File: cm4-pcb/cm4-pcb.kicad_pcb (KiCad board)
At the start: 2 copper layers, 140 x 70.5 mm, 41 parts, among them J1 Conn_01x02_Pin, J2 Conn_01x02_Pin, J3 USB1125-GF-B, J4 Conn_02x03_Odd_Even, J5 Conn_01x04, J6 Conn_01x04, J7 Conn_01x02, U1 Pfostenstecker_6_2x3, U2 Pfostenstecker_6_2x3, U3 TPD4EUSB30, U4 MagJack-A70-112-331N126, U5 SMD-PUSH-BTN, U6 TPD4EUSB30, U7 TPD4EUSB30

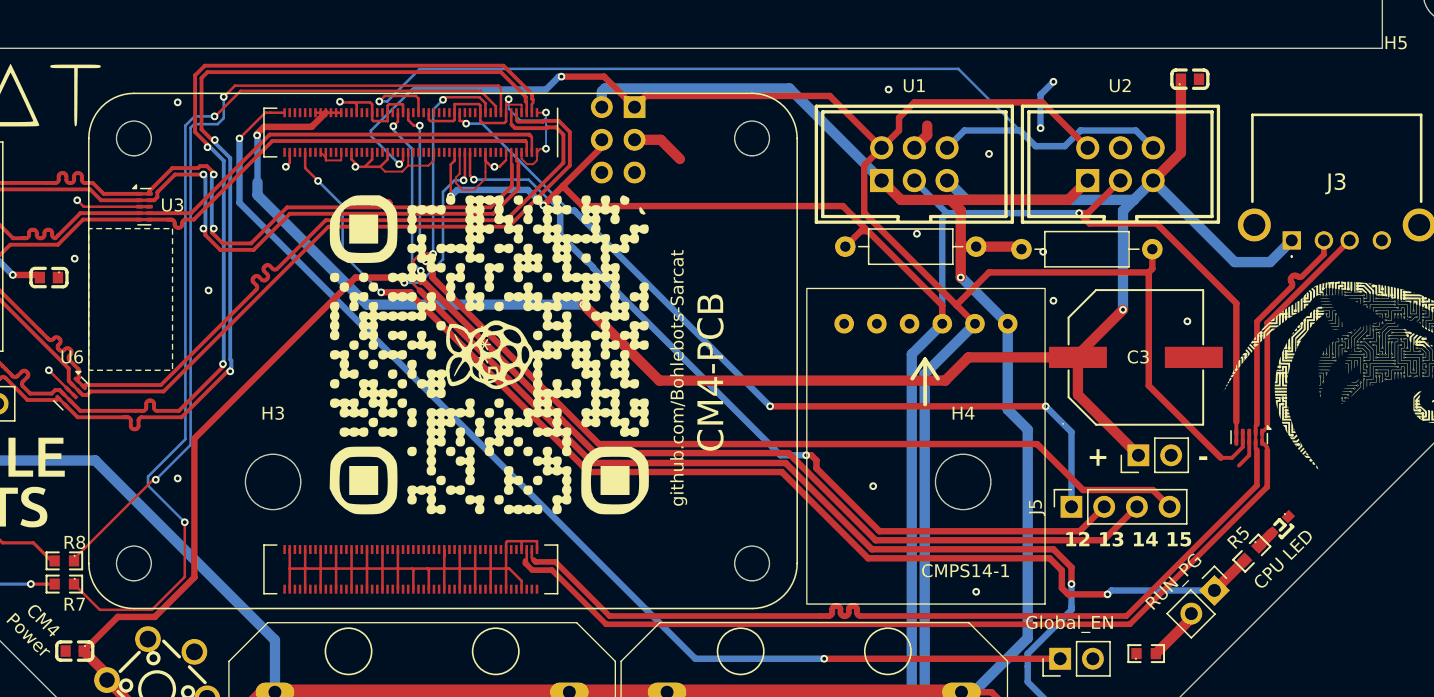
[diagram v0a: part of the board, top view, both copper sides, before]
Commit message: Moved Diff. Pair Routes for Crosstalk
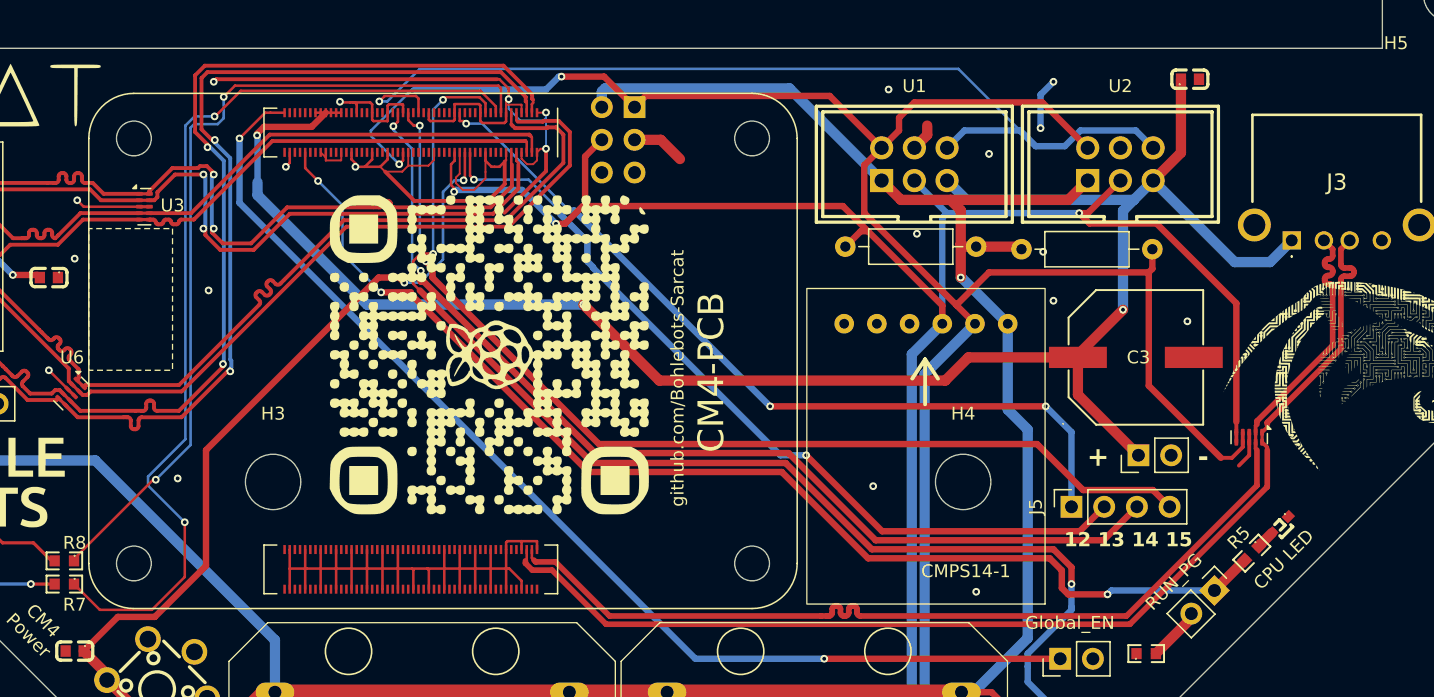
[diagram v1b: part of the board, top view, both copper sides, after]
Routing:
- net GND: track 203.1 -> 245.5 mm, vias 23 -> 22
- net USB_D+: track 87.2 -> 88.7 mm
- net USB_D-: track 87.1 -> 88.6 mm
- net SHUTDOWN: track 70.5 -> 69.5 mm
- net SCL: track 199.1 -> 199.7 mm

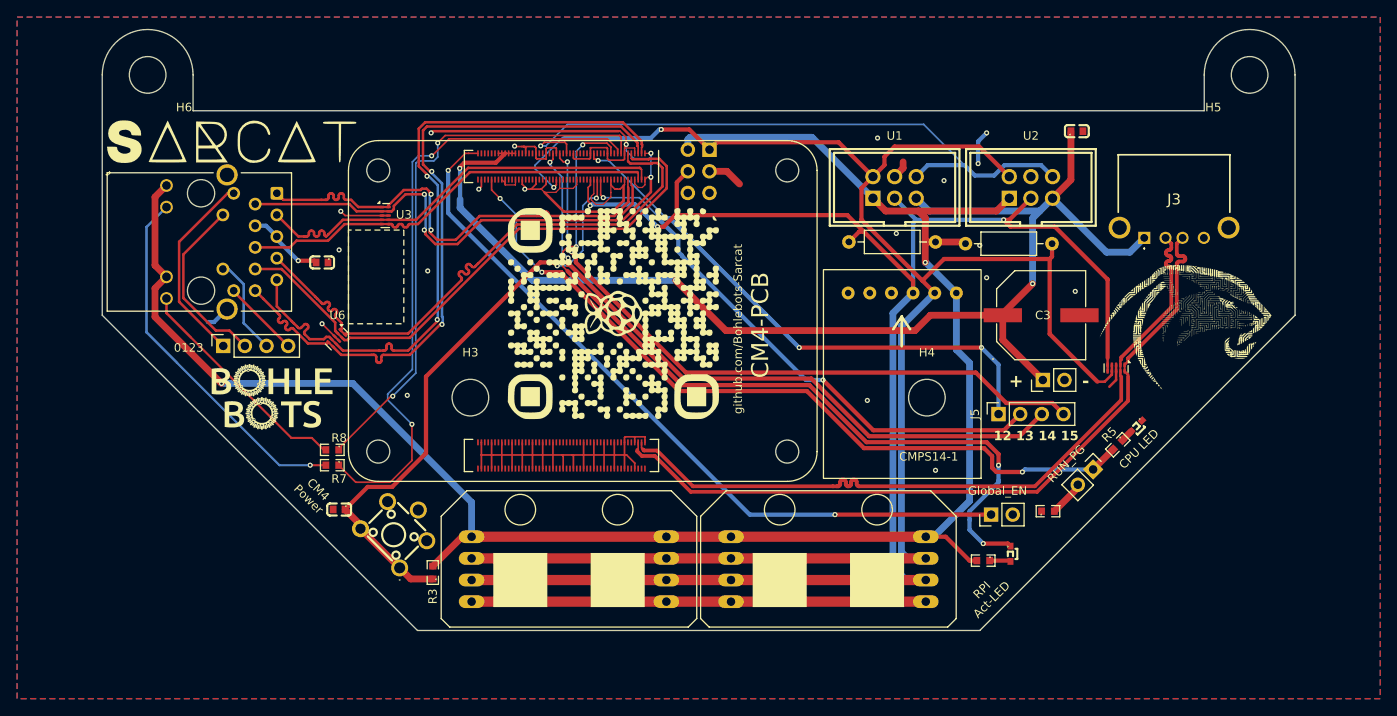
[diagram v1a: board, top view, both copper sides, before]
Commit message: Changed Ethernet Magjack + some layout changes
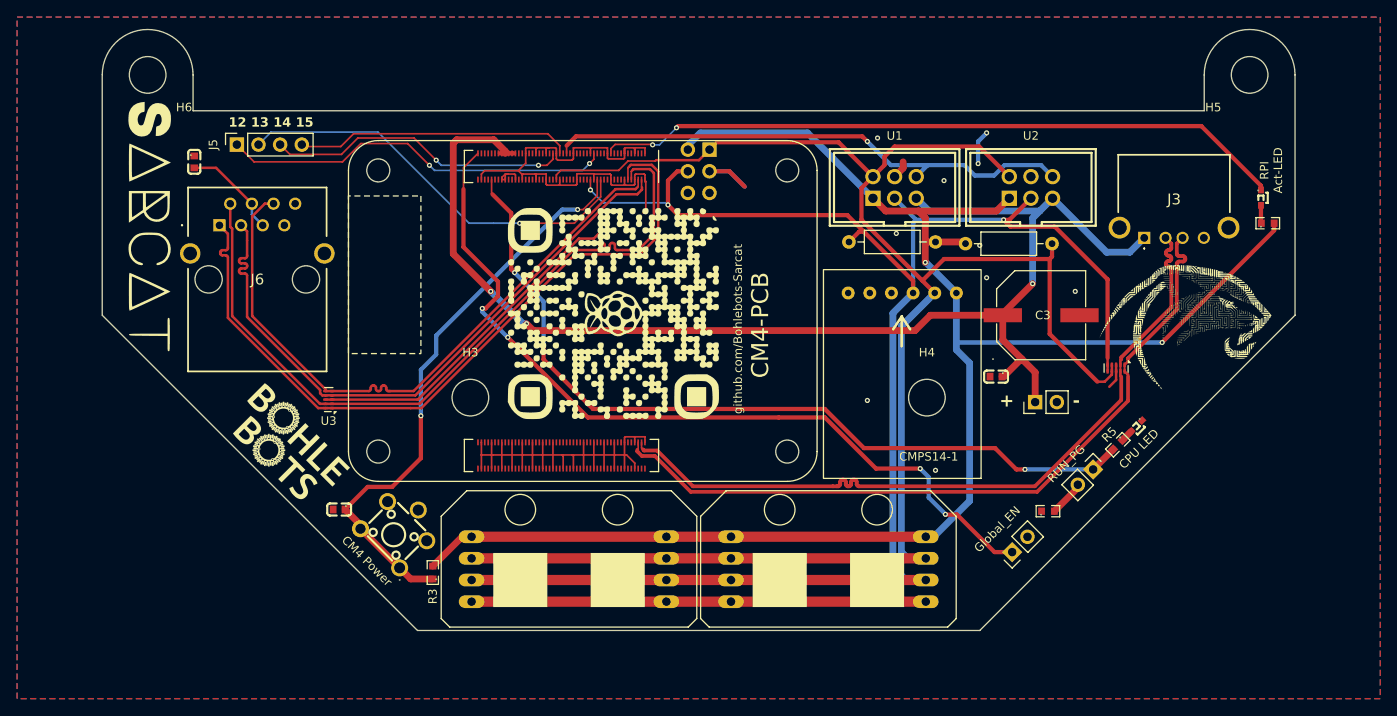
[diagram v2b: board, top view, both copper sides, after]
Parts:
- removed R7, R8: SMD-470R, BohleBots:R0603
- removed U4: MagJack-A70-112-331N126, CM4IO:TRJG0926HENL
- removed U6: TPD4EUSB30, Package_SON:USON-10_2.5x1.0mm_P0.5mm
- J6: value Conn_01x04 -> J0011D21NL; footprint Connector_PinSocket_2.54mm:PinSocket_1x04_P2.54mm_Vertical -> J0011D21NL:J0011D21NL
- moved J5 94.8 mm to (-54.2, 35.0)
- moved R6 51.8 mm to (66.8, 44.2), turned to 0 degrees
- moved ACT_LED1 51.1 mm to (66.0, 41.2)
- moved C4 30.3 mm to (34.9, 62.2), turned to 180 degrees
- moved U3 22.6 mm to (-43.4, 64.9), turned to 180 degrees
- moved C1 19.1 mm to (-59.2, 37.0), turned to -90 degrees
- moved J6 14.2 mm to (-56.2, 44.4), turned to 180 degrees
- moved G*** 13.9 mm to (-64.4, 44.6), turned to -90 degrees
- moved G*** 5.93 mm to (-48.3, 70.2), turned to -45 degrees
- moved J1 5.05 mm to (36.8, 82.8), turned to 135 degrees
- moved J7 2.75 mm to (39.5, 65.2)
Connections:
- C1 pad 2: Net-(C1-Pad2) -> Net-(J6-CT_1)
- J6 pad 1: /TR0_TAP -> /TRD0_P
- J6 pad 2: /TR1_TAP -> /TRD0_N
- J6 pad 3: /TR2_TAP -> /TRD1_P
- J6 pad 4: /TR3_TAP -> Net-(J6-CT_1)
- Module1 pad 11: /TRD2_P -> unconnected-(Module1A-Ethernet_Pair2_P-Pad11)
- Module1 pad 15: /ETH_LEDY -> unconnected-(Module1A-Ethernet_nLED3(3.3v)-Pad15)
- Module1 pad 17: /ETH_LEDG -> unconnected-(Module1A-Ethernet_nLED2(3.3v)-Pad17)
- Module1 pad 3: /TRD3_P -> unconnected-(Module1A-Ethernet_Pair3_P-Pad3)
- Module1 pad 5: /TRD3_N -> unconnected-(Module1A-Ethernet_Pair3_N-Pad5)
- Module1 pad 9: /TRD2_N -> unconnected-(Module1A-Ethernet_Pair2_N-Pad9)
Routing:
- net /TRD3_P: track 81.0 -> 0.00 mm, vias 2 -> 0
- net /TRD3_N: track 81.0 -> 0.00 mm, vias 2 -> 0
- net /ETH_LEDG: track 74.1 -> 0.00 mm, vias 2 -> 0
- net /TRD2_P: track 68.5 -> 0.00 mm
- net /TRD2_N: track 67.5 -> 0.00 mm
- net /ETH_LEDY: track 65.9 -> 0.00 mm, vias 2 -> 0
- net P15: track 78.5 -> 32.5 mm, vias 2 -> 0
- net P14: track 79.1 -> 35.6 mm
- net Net-(U4-LEDG_K): track 43.2 -> 0.00 mm, vias 1 -> 0
- net /TRD0_P: track 55.7 -> 88.9 mm, vias 2 -> 0
- net /TRD0_N: track 55.8 -> 88.8 mm, vias 2 -> 0
- net +3.3V: track 225.3 -> 194.5 mm
- net Net-(U4-LEDY_K): track 27.1 -> 0.00 mm
- net /TRD1_N: track 50.2 -> 76.3 mm
- net /TRD1_P: track 50.2 -> 75.5 mm
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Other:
- board text removed: "0123"

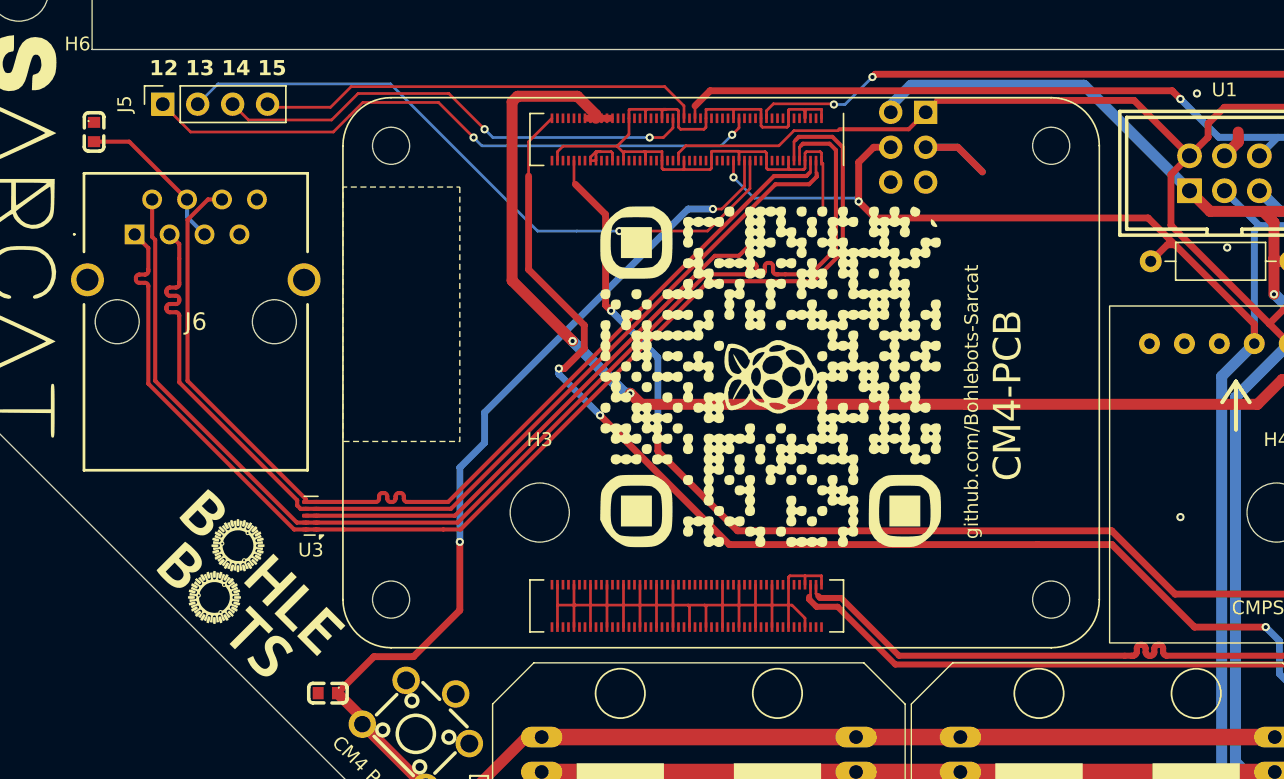
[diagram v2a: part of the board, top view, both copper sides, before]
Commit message: Adjusted GND Layer for Antenna
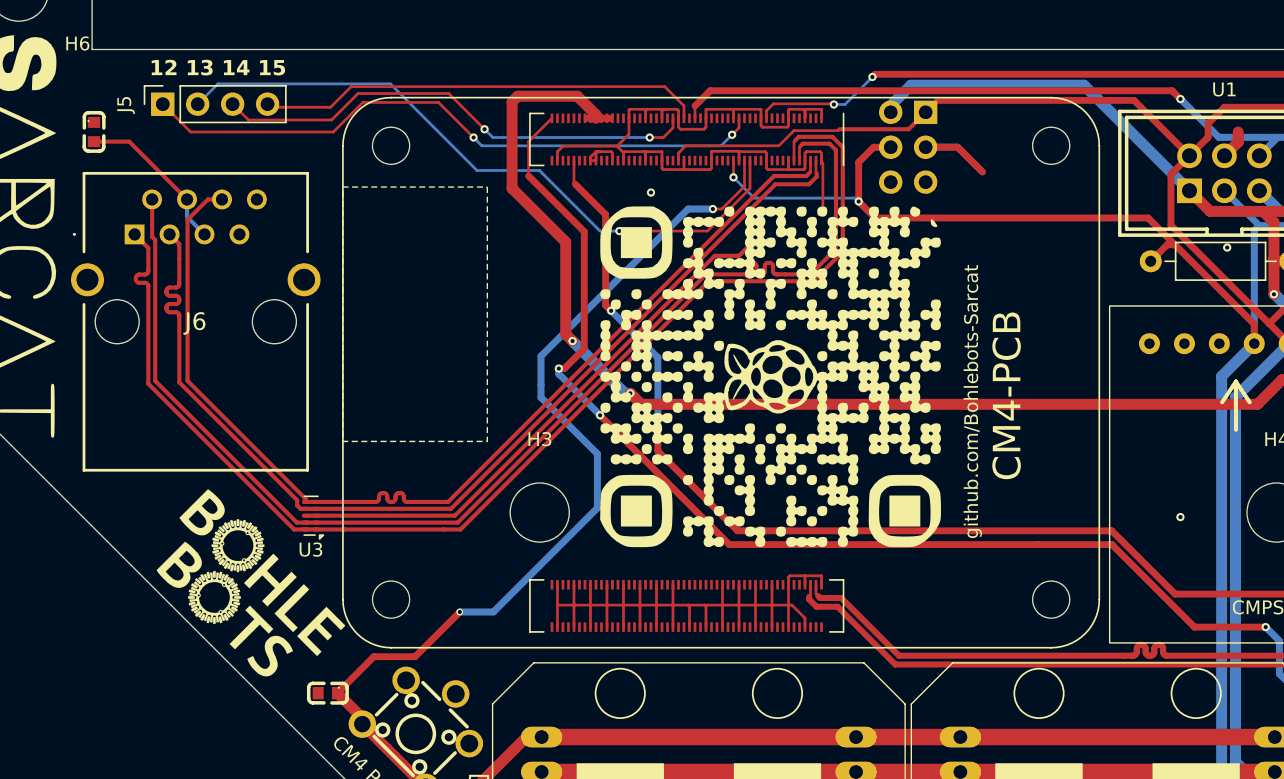
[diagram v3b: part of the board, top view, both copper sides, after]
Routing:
- net SHUTDOWN: track 68.0 -> 72.9 mm
- net GND: vias 11 -> 12
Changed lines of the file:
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@@
 		(attr smd)
 		(fp_rect
-			(start 3 -5)
+			(start 3 -7)
 			(end 21.5 3.5)
 			(stroke
@@
 		)
 		(fp_rect
-			(start 3 -5)
+			(start 3 -7)
 			(end 21.5 3.5)
 			(stroke
@@
 			(polygon
 				(pts
-					(xy -41.1 59.5) (xy -32.6 59.5) (xy -32.6 41) (xy -41.1 41)
+					(xy -41.1 59.5) (xy -30.6 59.5) (xy -30.6 41) (xy -41.1 41)
 				)
 			)
@@
 		(fp_arc
 			(start 1.390018 0.400203)
-			(mid 1.299267 0.61928)
+			(mid 1.299267 0.619284)
 			(end 1.080188 0.710033)
 			(stroke
@@
 			)
 		)
-		(property "Footprint" "USB1125GFB"
+		(property "Footprint" "USB1125-GF-B:USB1125GFB"
 			(at 0 0 180)
 			(unlocked yes)
@@
 		(fp_arc
 			(start 1.390018 0.400203)
-			(mid 1.299267 0.619284)
+			(mid 1.299267 0.61928)
 			(end 1.080188 0.710033)
 			(stroke
@@
 		)
 		(property "Value" "SMD-100R"
-			(at 0 2.660605 360)
+			(at 0 2.660605 0)
 			(layer "F.Fab")
 			(effects
@@
 		)
 		(fp_text user "REF**"
-			(at 0 4.660604 360)
+			(at 0 4.660604 0)
 			(layer "F.Fab")
 			(effects
@@
 		(tags "Through hole pin header THT 1x02 2.54mm single row")
 		(property "Reference" "J1"
-			(at -2.828427 1.131371 225)
+			(at -2.828427 1.131371 -135)
 			(layer "F.SilkS")
 			(hide yes)
@@
 		)
 		(fp_text user "${REFERENCE}"
-			(at 0 1.270001 225)
+			(at 0 1.270001 -135)
 			(layer "F.Fab")
 			(effects
@@
 			)
 		)
-		(property "Footprint" "J0011D21NL"
+		(property "Footprint" "J0011D21NL:J0011D21NL"
 			(at 0 0 180)
 			(unlocked yes)
@@
 		(fp_arc
 			(start 1.390018 0.400203)
-			(mid 1.299268 0.619285)
+			(mid 1.29927 0.619287)
 			(end 1.080188 0.710033)
 			(stroke
@@
 	)
 	(via
-		(at 21 34.2)
+		(at -18.7 41.4)
 		(size 0.6)
 		(drill 0.3)
@@
 	)
 	(via
+		(at -20 45.1)
+		(size 0.6)
+		(drill 0.3)
+		(layers "F.Cu" "B.Cu")
+		(net 1)
+	)
+	(via
 		(at -11.45 45.15)
 		(size 0.6)
@@
 	)
 	(segment
-		(start -21 44.2)
-		(end -24.1 44.2)
+		(start -22.4 44.2)
+		(end -21 44.2)
 		(width 0.2)
 		(layer "B.Cu")
@@
 	)
 	(segment
-		(start -51.66 34.975)
-		(end -50.185 33.5)
+		(start -50.185 33.5)
+		(end -37.645227 33.5)
 		(width 0.2)
 		(layer "B.Cu")
@@
 	(segment
 		(start -37.645227 33.5)
-		(end -26.945227 44.2)
+		(end -31.345227 39.8)
 		(width 0.2)
 		(layer "B.Cu")
@@
 	)
 	(segment
-		(start -26.945227 44.2)
-		(end -24.1 44.2)
+		(start -51.66 34.975)
+		(end -50.185 33.5)
 		(width 0.2)
 		(layer "B.Cu")
@@
 	)
 	(segment
-		(start -50.185 33.5)
-		(end -37.645227 33.5)
+		(start -26.8 39.8)
+		(end -22.4 44.2)
+		(width 0.2)
+		(layer "B.Cu")
+		(net 15)
+	)
+	(segment
+		(start -31.345227 39.8)
+		(end -26.8 39.8)
 		(width 0.2)
 		(layer "B.Cu")
@@
 	)
 	(segment
+		(start -24.9 45)
+		(end -28.8 41.1)
+		(width 0.8)
+		(layer "F.Cu")
+		(net 29)
+	)
+	(segment
 		(start 35.700127 57.900127)
 		(end 37.9 60.1)
@@
 	)
 	(segment
-		(start -24.4 52.2)
-		(end -28.8 47.8)
+		(start -28.8 34.8)
+		(end -28.4 34.4)
 		(width 0.8)
 		(layer "F.Cu")
@@
 	)
 	(segment
+		(start -22.7 35.75)
+		(end -22.7 36)
+		(width 0.8)
+		(layer "F.Cu")
+		(net 29)
+	)
+	(segment
 		(start -21.9 36)
 		(end -21.65 36)
@@
 	)
 	(segment
-		(start -28.4 34.4)
-		(end -24.05 34.4)
-		(width 0.8)
-		(layer "F.Cu")
-		(net 29)
-	)
-	(segment
 		(start 4.2 56.8)
 		(end -19.4 56.8)
@@
 	)
 	(segment
-		(start 37.9 60.1)
-		(end 39.5 61.7)
+		(start -28.8 41.1)
+		(end -28.8 34.8)
 		(width 0.8)
 		(layer "F.Cu")
@@
 	)
 	(segment
-		(start 35.700127 55)
-		(end 35.700127 54.799772)
+		(start 37.9 60.1)
+		(end 39.5 61.7)
 		(width 0.8)
 		(layer "F.Cu")
@@
 	)
 	(segment
-		(start -22.7 35.75)
-		(end -22.7 36)
+		(start 35.700127 55)
+		(end 35.700127 54.799772)
 		(width 0.8)
 		(layer "F.Cu")
@@
 	)
 	(segment
-		(start -24.05 34.4)
-		(end -22.7 35.75)
-		(width 0.8)
-		(layer "F.Cu")
-		(net 29)
-	)
-	(segment
-		(start -28.8 47.8)
-		(end -28.8 34.8)
+		(start -24.4 52.2)
+		(end -24.9 51.7)
 		(width 0.8)
 		(layer "F.Cu")
@@
 	)
 	(segment
+		(start -28.4 34.4)
+		(end -24.05 34.4)
+		(width 0.8)
+		(layer "F.Cu")
+		(net 29)
+	)
+	(segment
 		(start -23.1 36)
 		(end -23.35 36)
@@
 	)
 	(segment
-		(start -28.8 34.8)
-		(end -28.4 34.4)
+		(start -24.05 34.4)
+		(end -22.7 35.75)
 		(width 0.8)
 		(layer "F.Cu")
@@
 		(net 29)
 	)
+	(segment
+		(start -24.9 51.7)
+		(end -24.9 45)
+		(width 0.8)
+		(layer "F.Cu")
+		(net 29)
+	)
 	(via
 		(at -20.2 56)
@@
 	)
 	(segment
-		(start 30.325 78.4)
-		(end 29 78.4)
+		(start -25 54.2)
+		(end -25.4 54.2)
 		(width 0.5)
 		(layer "F.Cu")
@@
 	)
 	(segment
-		(start -27.6 47)
-		(end -23.549999 51.050001)
+		(start 30.325 78.4)
+		(end 29 78.4)
 		(width 0.5)
 		(layer "F.Cu")
@@
 	)
 	(segment
-		(start -23.549999 51.050001)
-		(end -23.549999 52.749999)
-		(width 0.5)
-		(layer "F.Cu")
-		(net 59)
-	)
-	(segment
 		(start -25.9 36)
 		(end -27.6 37.7)
@@
 	)
 	(segment
+		(start -27.6 40.2)
+		(end -23.549999 44.250001)
+		(width 0.5)
+		(layer "F.Cu")
+		(net 59)
+	)
+	(segment
 		(start 14.8201 67)
 		(end 20.8201 73)
@@
 	)
 	(segment
-		(start -25 54.2)
-		(end -25.4 54.2)
-		(width 0.5)
-		(layer "F.Cu")
-		(net 59)
-	)
-	(segment
-		(start -23.549999 52.749999)
-		(end -25 54.2)
+		(start -23.549999 44.250001)
+		(end -23.549999 52.749999)
 		(width 0.5)
 		(layer "F.Cu")
@@
 	)
 	(segment
-		(start -27.6 40.2)
-		(end -27.6 47)
+		(start -22.4 57.6)
+		(end -13 67)
 		(width 0.5)
 		(layer "F.Cu")
@@
 	)
 	(segment
-		(start -22.4 57.6)
-		(end -13 67)
+		(start -23.549999 52.749999)
+		(end -25 54.2)
 		(width 0.5)
 		(layer "F.Cu")
@@
 	)
 	(segment
-		(start -35.972182 75.15)
-		(end -32.6 71.777818)
-		(width 0.5)
-		(layer "F.Cu")
-		(net 143)
-	)
-	(segment
 		(start -13.551471 42.6)
 		(end -11.9 40.948529)
@@
 	)
 	(segment
-		(start -35.972182 75.15)
-		(end -38.849976 75.15)
+		(start -38.849976 75.15)
+		(end -35.85 75.15)
 		(width 0.5)
 		(layer "F.Cu")
@@
 	)
 	(segment
-		(start -38.849976 75.15)
-		(end -41.499976 77.8)
-		(width 0.5)
-		(layer "F.Cu")
-		(net 143)
-	)
-	(segment
 		(start -11.9 40.948529)
 		(end -11.9 39.08)
@@
 	)
 	(segment
+		(start -41.499976 77.8)
+		(end -38.849976 75.15)
+		(width 0.5)
+		(layer "F.Cu")
+		(net 143)
+	)
+	(segment
 		(start -13.551471 42.6)
 		(end -14.2 42.6)
@@
 	)
 	(segment
-		(start -32.6 71.777818)
-		(end -32.6 66.8)
+		(start -35.85 75.15)
+		(end -32.6 71.9)
 		(width 0.5)
 		(layer "F.Cu")
@@
 	)
 	(via
-		(at -32.6 66.8)
-		(size 0.6)
+		(at -32.6 71.9)
+		(size 0.5)
 		(drill 0.3)
 		(layers "F.Cu" "B.Cu")
@@
 	)
 	(segment
-		(start -32.6 66.8)
-		(end -32.6 61.4)
+		(start -22.6 64.340803)
+		(end -30.159197 71.9)
 		(width 0.5)
 		(layer "B.Cu")
@@
 	)
 	(segment
-		(start -30.8 57.4)
-		(end -30.8 57.397918)
+		(start -16.002082 42.6)
+		(end -26.7 53.297918)
 		(width 0.5)
 		(layer "B.Cu")
@@
 	)
 	(segment
-		(start -16.002082 42.6)
-		(end -14.2 42.6)
+		(start -26.7 56.3)
+		(end -22.6 60.4)
 		(width 0.5)
 		(layer "B.Cu")
@@
 	)
 	(segment
-		(start -30.8 59.6)
-		(end -30.8 57.4)
+		(start -26.7 53.297918)
+		(end -26.7 55.4)
 		(width 0.5)
 		(layer "B.Cu")
@@
 	)
 	(segment
-		(start -32.6 61.4)
-		(end -30.8 59.6)
+		(start -22.6 60.4)
+		(end -22.6 64.340803)
 		(width 0.5)
 		(layer "B.Cu")
@@
 	)
 	(segment
-		(start -30.8 57.397918)
+		(start -26.7 55.4)
+		(end -26.7 56.3)
+		(width 0.5)
+		(layer "B.Cu")
+		(net 143)
+	)
+	(segment
+		(start -14.2 42.6)
 		(end -16.002082 42.6)
 		(width 0.5)
 		(layer "B.Cu")
+		(net 143)
+	)
+	(segment
+		(start -30.159197 71.9)
+		(end -32.6 71.9)
+		(width 0.5)
+		(layer "B.Cu")
